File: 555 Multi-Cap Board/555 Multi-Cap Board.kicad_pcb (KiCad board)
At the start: 2 copper layers, 33 x 27 mm, 20 parts, among them J1 PWR, J2 OUT, U1 bald_LM555xM

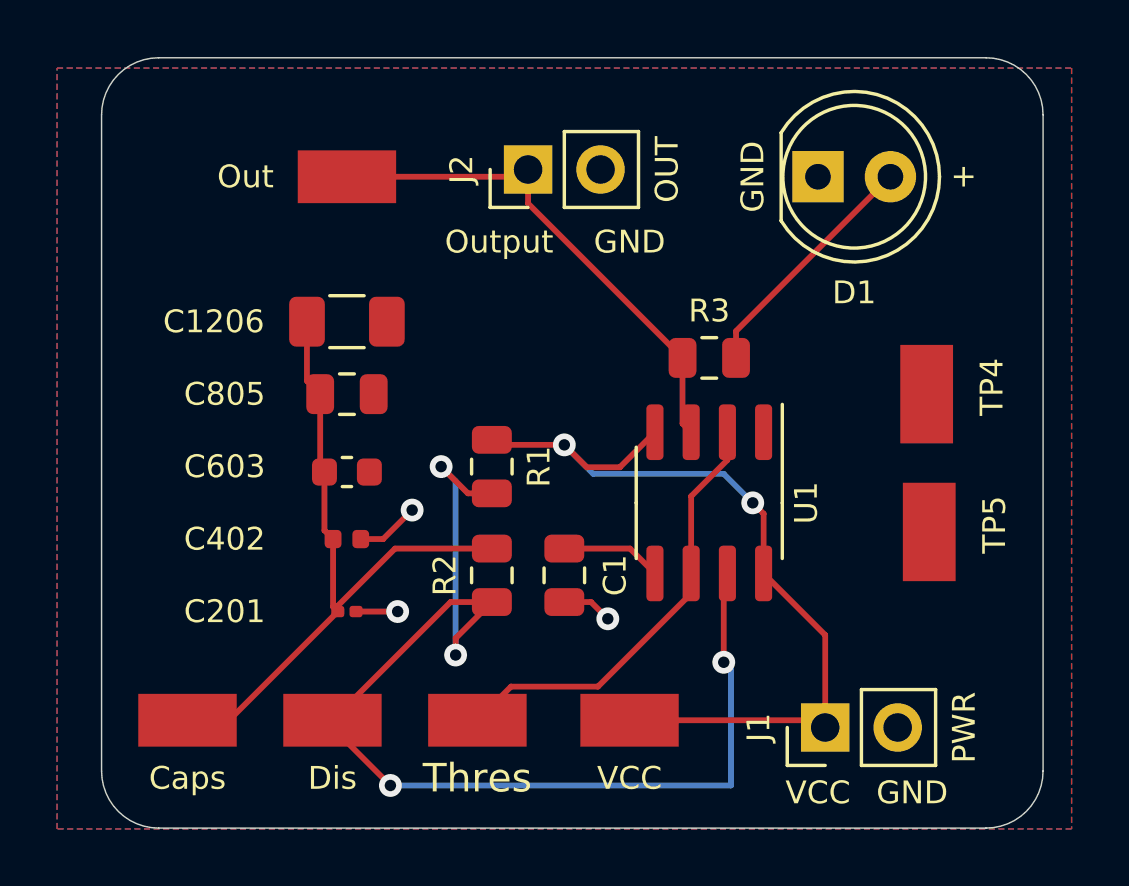
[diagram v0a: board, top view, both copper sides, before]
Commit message: added values for video
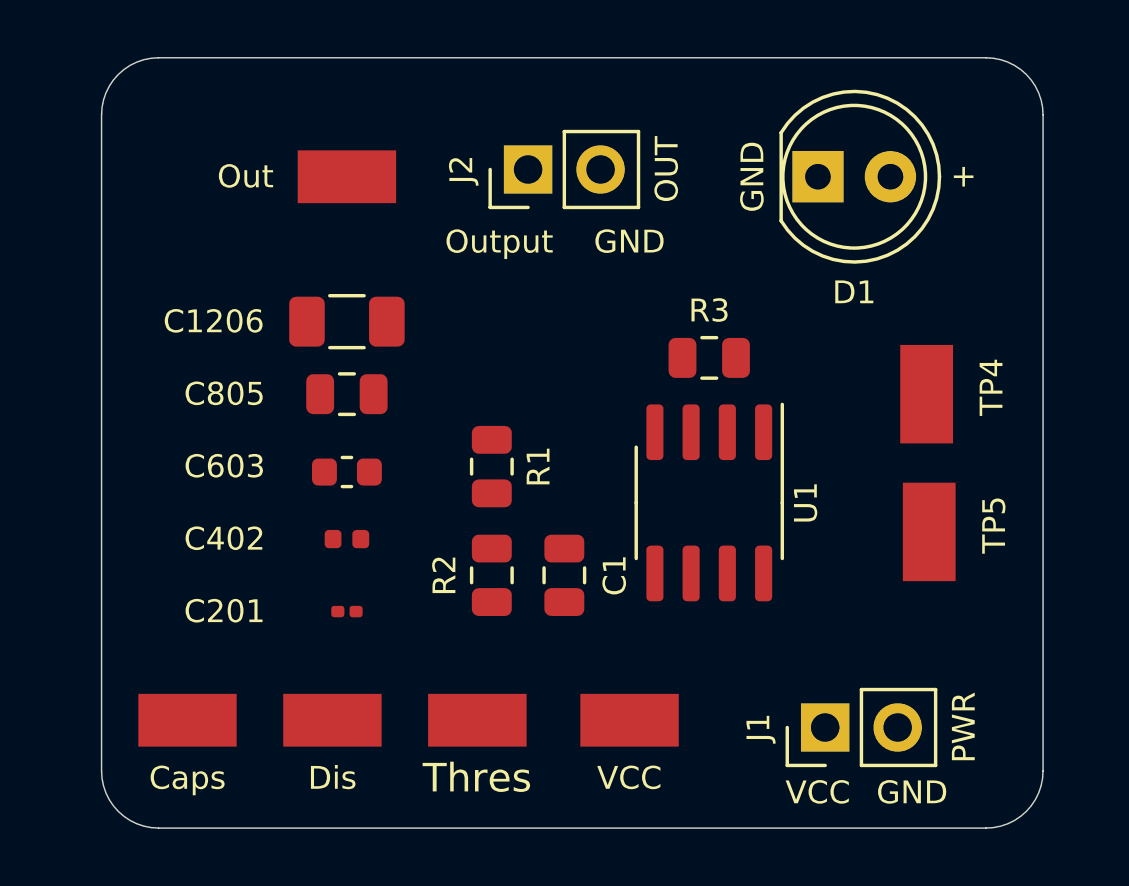
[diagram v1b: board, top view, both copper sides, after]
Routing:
- net Net-(R1-Pad2): track 41.3 -> 0.00 mm, vias 4 -> 0
- net VCC: track 30.0 -> 0.00 mm, vias 2 -> 0
- net Net-(C1206-Pad1): track 23.9 -> 0.00 mm
- net /Output: track 18.0 -> 0.00 mm
- net Net-(TP7-Pad1): track 15.5 -> 0.00 mm
- net Net-(D1-Pad2): track 8.59 -> 0.00 mm
- net GND: track 5.45 -> 0.00 mm, vias 3 -> 0
- net Net-(C1-Pad1): track 3.54 -> 0.00 mm
- removed copper zone on B.Cu, net GND
- removed copper zone on F.Cu, net GND
